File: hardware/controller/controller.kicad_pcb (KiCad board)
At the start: 2 copper layers, 30 parts, among them J1 Conn_01x02_Pin, J10 Conn_01x04_Pin, J11 Barrel_Jack, J2 Conn_01x02_Pin, J3 Conn_01x02_Pin, J4 Conn_01x02_Pin, J5 Screw_Terminal_01x02, J6 Screw_Terminal_01x02, J7 Conn_01x04_Pin, J8 Conn_01x04_Pin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

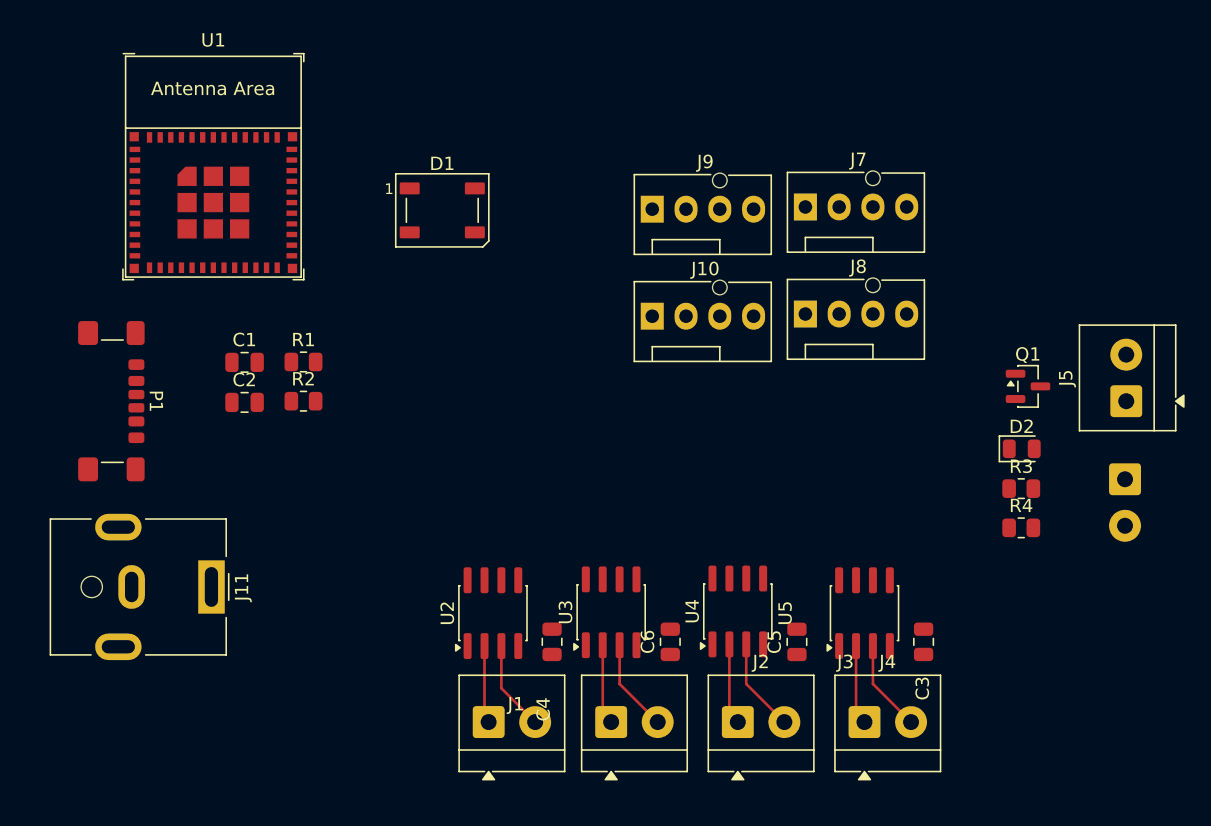
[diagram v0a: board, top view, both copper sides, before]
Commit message: Fixed up MCU strapping pins
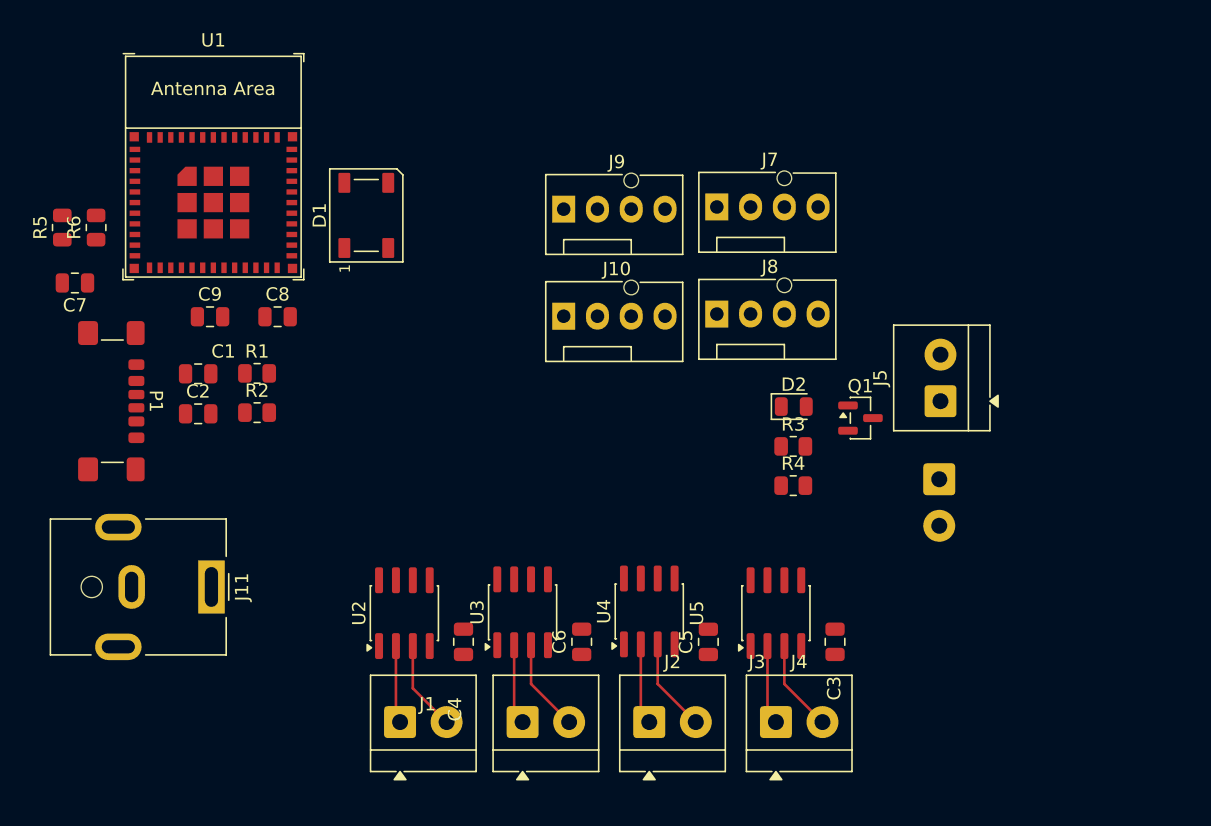
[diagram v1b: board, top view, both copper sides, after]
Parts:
- added C7: 10uF, Capacitor_SMD:C_0805_2012Metric, F.Cu at (110.2, 81.3)
- added C8: 1uF, Capacitor_SMD:C_0805_2012Metric, F.Cu at (125.4, 83.8)
- added C9: 0.1uf, Capacitor_SMD:C_0805_2012Metric, F.Cu at (120.3, 83.8)
- added R5: 10K, Resistor_SMD:R_0805_2012Metric, F.Cu at (109.2, 77.1)
- added R6: R_US, Resistor_SMD:R_0805_2012Metric, F.Cu at (111.8, 77.1)
- moved R3 17.4 mm to (164.2, 93.6)
- moved D2 17.4 mm to (164.2, 90.6)
- moved R4 17.4 mm to (164.2, 96.5)
- moved J5 14.0 mm to (175.3, 90.2)
- moved J6 14.0 mm to (175.2, 96.0)
- moved Q1 12.8 mm to (169.2, 91.4)
- moved C4 6.66 mm to (139.4, 108.3)
- moved C3 6.66 mm to (167.3, 108.3)
- moved C5 6.66 mm to (157.8, 108.3)
- moved C6 6.66 mm to (148.3, 108.3)
- moved J1 6.66 mm to (134.6, 114.3)
- moved J10 6.66 mm to (146.9, 83.8)
- moved J2 6.66 mm to (143.8, 114.3)
- moved J3 6.66 mm to (153.4, 114.3)
- moved J4 6.66 mm to (162.9, 114.3)
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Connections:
- C1 pad 1: /Microcontroller/D- -> Net-(P1-D-)
- C2 pad 1: /Microcontroller/D+ -> Net-(P1-D+)
- R1 pad 1: Net-(U1-GPIO19/USB_D+) -> /Microcontroller/USB_D-
- R1 pad 2: /Microcontroller/D+ -> Net-(P1-D-)
- R2 pad 1: Net-(U1-GPIO18/USB_D-) -> /Microcontroller/USB_D+
- R2 pad 2: /Microcontroller/D- -> Net-(P1-D+)
- U1 pad 26: Net-(U1-GPIO18/USB_D-) -> /Microcontroller/USB_D-
- U1 pad 27: Net-(U1-GPIO19/USB_D+) -> /Microcontroller/USB_D+
- U1 pad 5: unconnected-(U1-GPIO2/ADC1_CH2-Pad5) -> Net-(U1-GPIO2/ADC1_CH2)
- U1 pad 8: unconnected-(U1-EN/CHIP_PU-Pad8) -> Net-(U1-EN/CHIP_PU)

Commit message: Filled out power section of schematic
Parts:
- removed Q1: MMBF4392, Package_TO_SOT_SMD:SOT-23
- added C10: 22uF, Capacitor_SMD:C_0805_2012Metric, F.Cu at (130.2, 91.2)
- added C11: 10uF, Capacitor_SMD:C_0805_2012Metric, F.Cu at (130.2, 94.2)
- added R10: 100k, Resistor_SMD:R_0805_2012Metric, F.Cu at (135.0, 92.1)
- added R4: 33k, Resistor_SMD:R_0805_2012Metric, F.Cu at (135.0, 83.2)
- added R7: 5.1k, Resistor_SMD:R_0805_2012Metric, F.Cu at (119.4, 94.0)
- added R8: 75k, Resistor_SMD:R_0805_2012Metric, F.Cu at (135.0, 86.2)
- added R9: 75k, Resistor_SMD:R_0805_2012Metric, F.Cu at (135.0, 89.1)
- added U6: TPS1H200AQDGNRQ1, TPS1H200:SOP65P490X110-9N, F.Cu at (168.6, 92.5)
- added U7: MPM3606AGQV-P, MPM3606:QFN3p0x5p0x1p6_MPM3606A_MNP, F.Cu at (127.4, 100.1)
- added U8: LM73100RPWR, LM73100:IC_LM73100RPWR, F.Cu at (130.8, 83.7)
- added U9: LM73100RPWR, LM73100:IC_LM73100RPWR, F.Cu at (130.8, 87.7)
- C3, C4, C5, C6: value C -> 0.1uf
- R1, R2: value R_US -> 33
- R3, R4: value R_US -> 500
- R6: value R_US -> 10k
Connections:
- J6 pad 1: +12V -> Net-(J6-Pin_1)
- J6 pad 2: Net-(J6-Pin_2) -> GND
- P1 pad A5: unconnected-(P1-CC-PadA5) -> Net-(P1-CC)

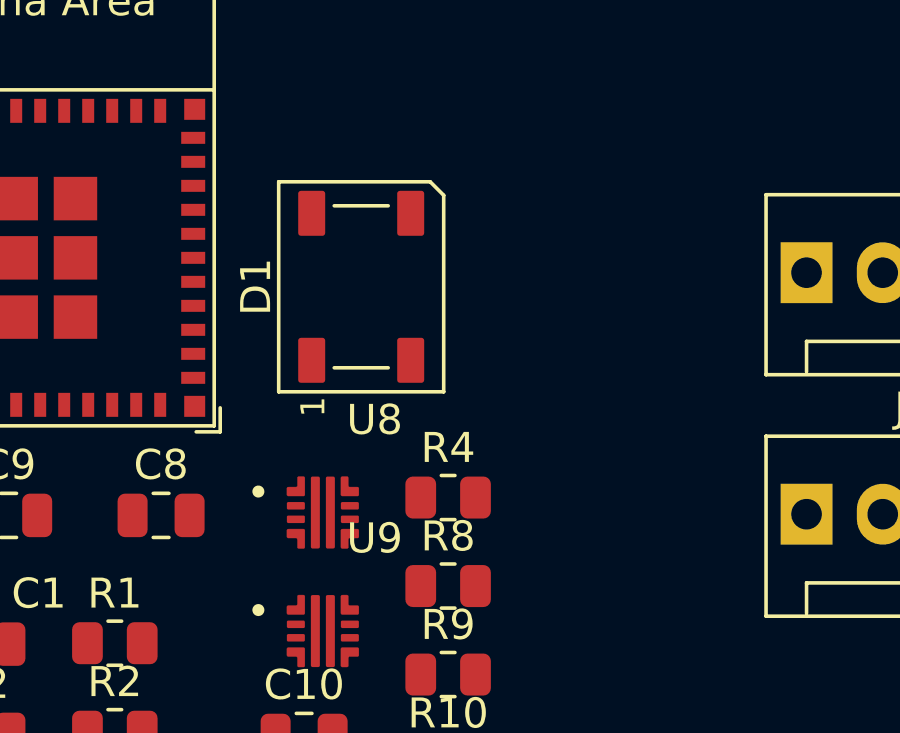
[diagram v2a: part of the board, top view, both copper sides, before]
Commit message: Fix USB symbol, adjust decoupling caps
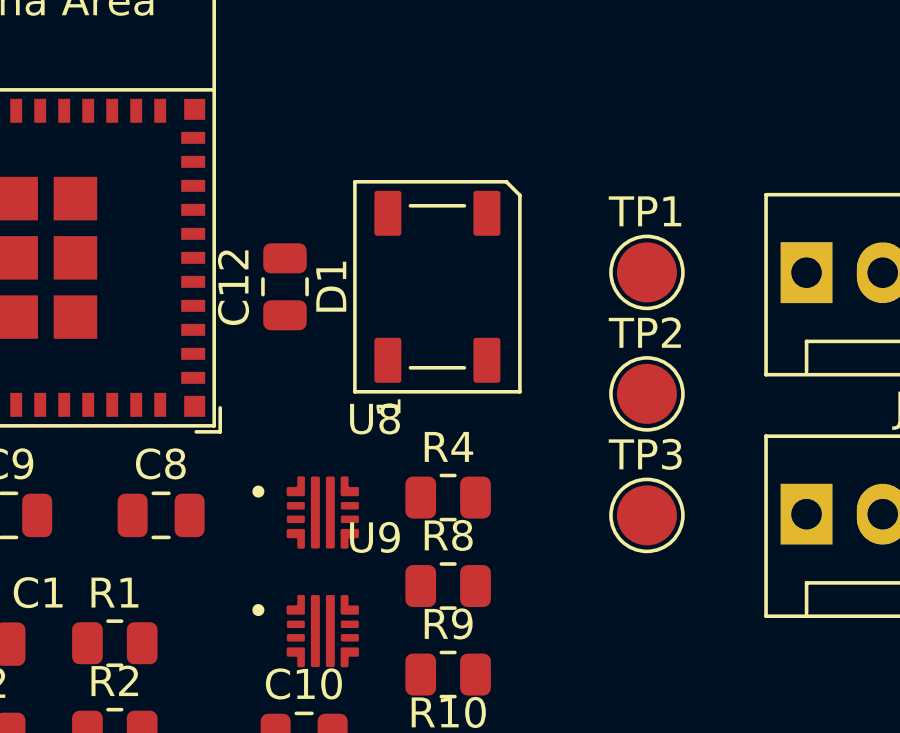
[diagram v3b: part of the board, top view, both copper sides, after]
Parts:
- added C12: 0.1uf, Capacitor_SMD:C_0805_2012Metric, F.Cu at (129.5, 76.2)
- added TP1: TestPoint, TestPoint:TestPoint_Pad_D2.0mm, F.Cu at (141.6, 75.7)
- added TP2: TestPoint, TestPoint:TestPoint_Pad_D2.0mm, F.Cu at (141.6, 79.8)
- added TP3: TestPoint, TestPoint:TestPoint_Pad_D2.0mm, F.Cu at (141.6, 83.8)
- moved D1 2.54 mm to (134.6, 76.2)
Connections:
- P1 pad A12: GND -> Net-(P1-GND-PadA1)
- P1 pad B12: GND -> Net-(P1-GND-PadA1)
- P1 pad S1: GND -> unconnected-(P1-SHIELD-PadS1)
- U6 pad 2: unconnected-(U6-DIAG_EN-Pad2) -> /Microcontroller/HEATER
- U6 pad 9: unconnected-(U6-EP-Pad9) -> GND
- U7 pad 4: unconnected-(U7-SW-Pad4) -> /Power/V_SW
- U7 pad 5: unconnected-(U7-SW-Pad5) -> /Power/V_SW
- U7 pad 6: unconnected-(U7-SW-Pad6) -> /Power/V_SW

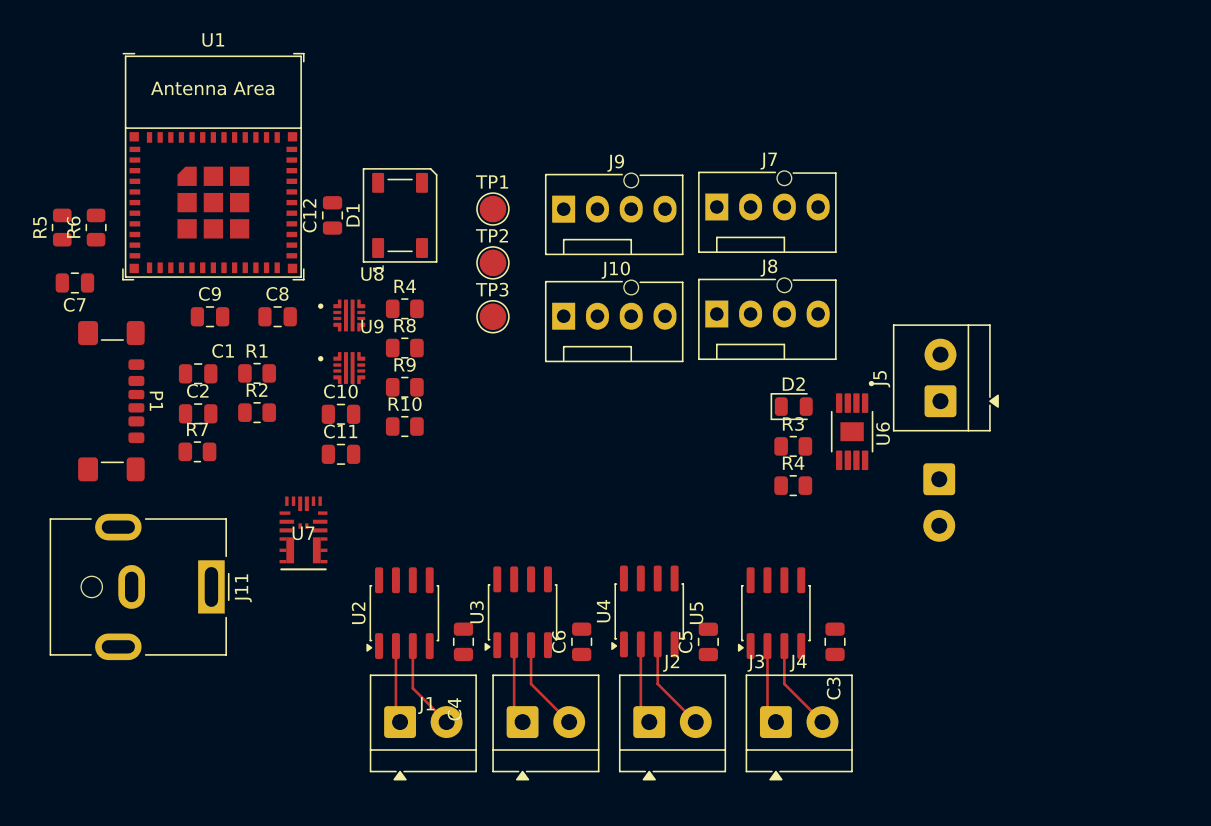
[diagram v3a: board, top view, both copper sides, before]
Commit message: Drop to 3x thermocouples, 2x fans
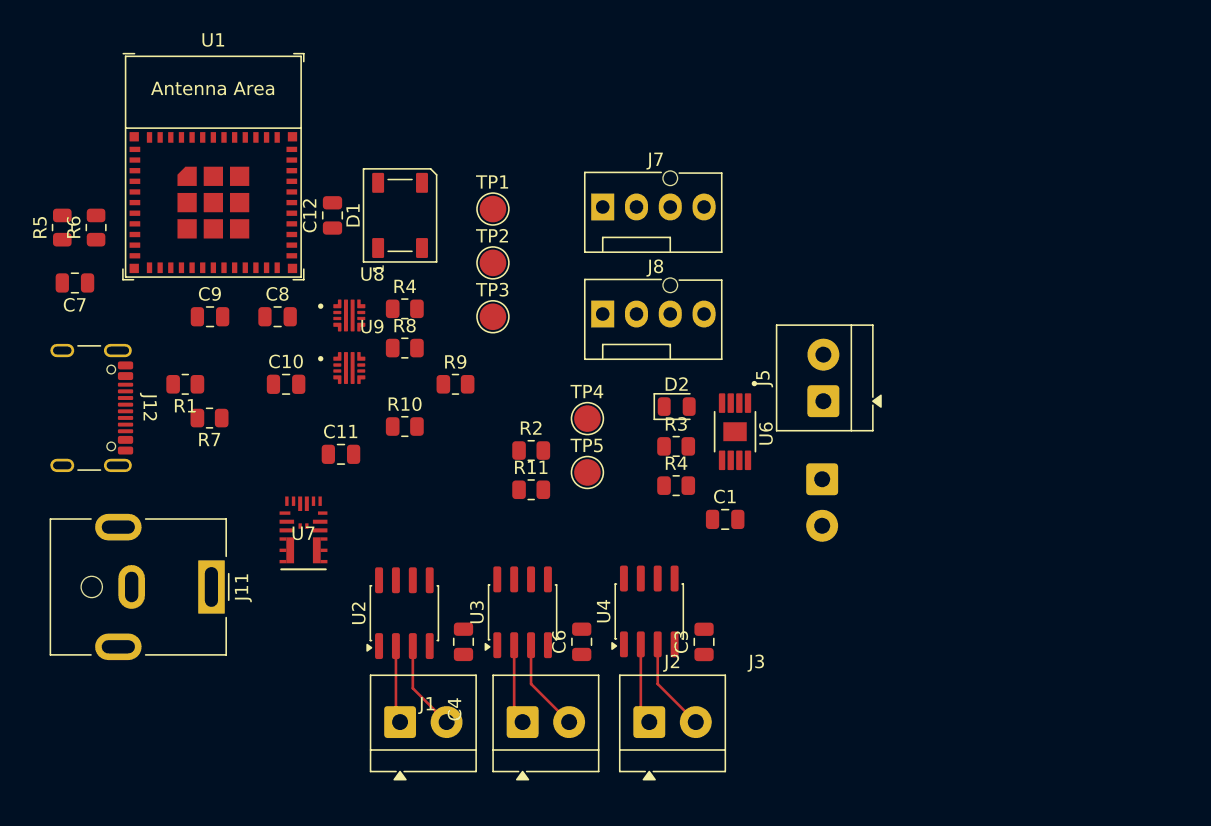
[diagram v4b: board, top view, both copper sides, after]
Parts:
- removed C2: C, Capacitor_SMD:C_0805_2012Metric
- removed C5: 0.1uf, Capacitor_SMD:C_0805_2012Metric
- removed J10, J9: Conn_01x04_Pin, Connector:FanPinHeader_1x04_P2.54mm_Vertical
- removed J4: Conn_01x02_Pin, TerminalBlock_4Ucon:TerminalBlock_4Ucon_1x02_P3.50mm_Horizontal
- removed P1: USB_C_Plug_USB2.0, Connector_USB:USB_C_Receptacle_GCT_USB4135-GF-A_6P_TopMnt_Horizontal
- removed U5: MAX31855KASA, Package_SO:SOIC-8_3.9x4.9mm_P1.27mm
- added J12: USB_C_Receptacle_USB2.0_14P, Connector_USB:USB_C_Receptacle_GCT_USB4105-xx-A_16P_TopMnt_Horizontal, F.Cu at (110.3, 90.7)
- added R11: 10k, Resistor_SMD:R_0805_2012Metric, F.Cu at (144.5, 96.8)
- added TP4: TestPoint, TestPoint:TestPoint_Pad_D2.0mm, F.Cu at (148.7, 91.5)
- added TP5: TestPoint, TestPoint:TestPoint_Pad_D2.0mm, F.Cu at (148.7, 95.5)
- C1: value C -> 0.1uF
- C12, C3, C4, C6: value 0.1uf -> 1uF
- R1: value 33 -> 5.1k
- R2: value 33 -> 10k
- moved C1 41.1 mm to (159.1, 99.1)
- moved R2 20.8 mm to (144.5, 93.9)
- moved C3 9.85 mm to (157.5, 108.3)
- moved R3 8.81 mm to (155.4, 93.6)
- moved R4 8.81 mm to (155.4, 96.5)
- moved U6 8.81 mm to (159.8, 92.5)
- moved D2 8.80 mm to (155.4, 90.6)
- moved J5 8.80 mm to (166.5, 90.2)
- moved J6 8.80 mm to (166.4, 96.0)
- moved J7 8.58 mm to (149.9, 75.6)
- moved J8 8.58 mm to (149.9, 83.6)
- moved R1 5.46 mm to (118.5, 88.9), turned to 180 degrees
- moved C10 4.70 mm to (126.0, 88.9)
- moved R9 3.82 mm to (138.8, 88.9)
- moved R7 2.70 mm to (120.3, 91.4), turned to 180 degrees
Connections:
- C1 pad 1: Net-(P1-D-) -> +12V
- J7 pad 3: unconnected-(J7-Pin_3-Pad3) -> FAN_0_TACH
- J8 pad 3: unconnected-(J8-Pin_3-Pad3) -> FAN_1_TACH
- R1 pad 1: /Microcontroller/USB_D- -> GND
- R1 pad 2: Net-(P1-D-) -> Net-(J12-CC1)
- R2 pad 1: /Microcontroller/USB_D+ -> FAN_0_TACH
- R2 pad 2: Net-(P1-D+) -> +3V3
- U1 pad 16: CS3 -> SO
- U1 pad 30: unconnected-(U1-GPIO20/U0RXD-Pad30) -> FAN_1_TACH
- U1 pad 31: unconnected-(U1-GPIO21/U0TXD-Pad31) -> FAN_0_TACH
- U1 pad 6: SO -> unconnected-(U1-GPIO3/ADC1_CH3-Pad6)
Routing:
- net Net-(J4-Pin_2): track 6.90 -> 0.00 mm
- net Net-(J4-Pin_1): track 5.98 -> 0.00 mm

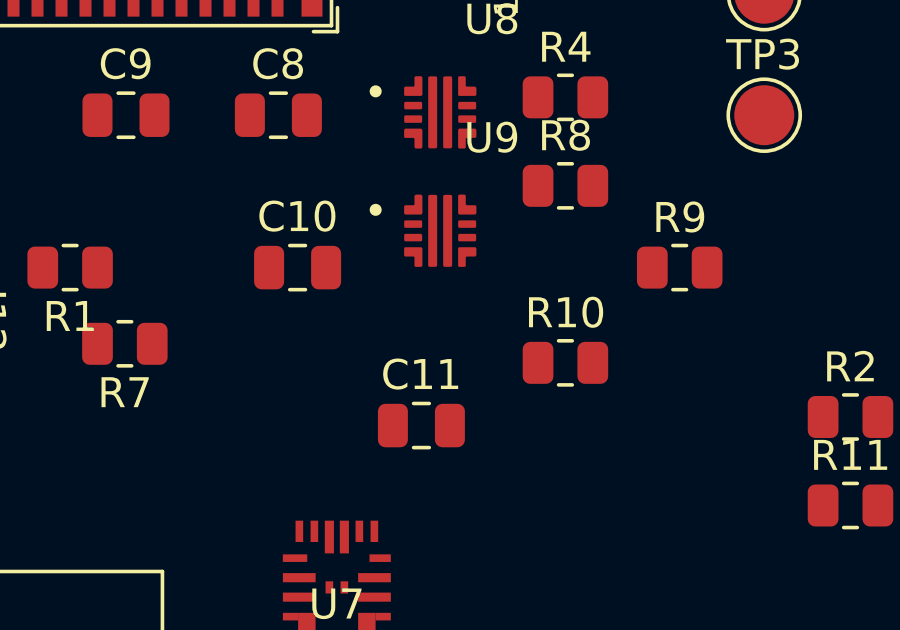
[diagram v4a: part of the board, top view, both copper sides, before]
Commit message: Add more decoupling caps
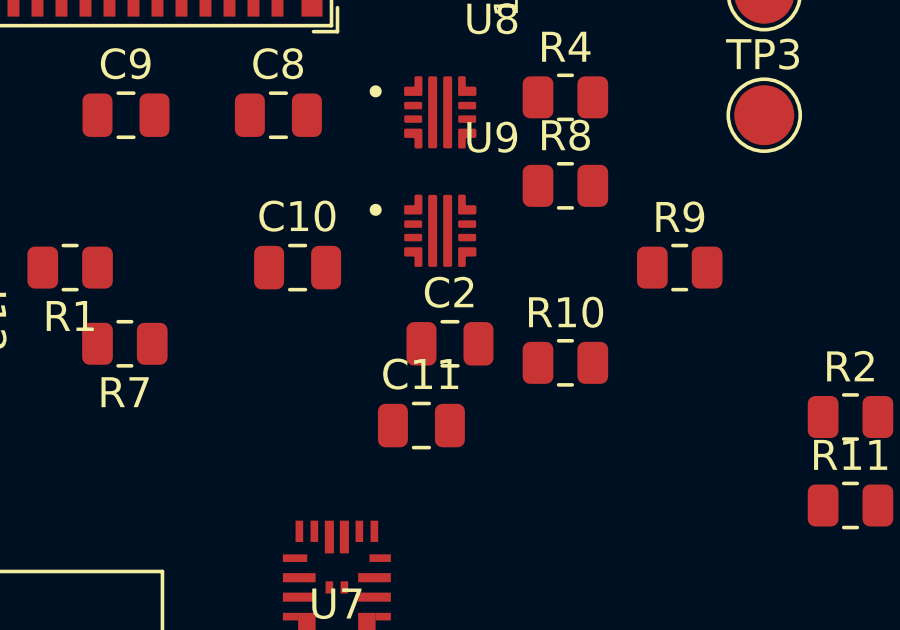
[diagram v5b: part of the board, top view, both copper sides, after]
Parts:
- added C2: 10uF, Capacitor_SMD:C_0805_2012Metric, F.Cu at (131.1, 91.4)
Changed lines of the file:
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@@
+		)
+	)
+	(footprint "Capacitor_SMD:C_0805_2012Metric"
+		(layer "F.Cu")
+		(at 131.13 91.44)
+		(descr "Capacitor SMD 0805 (2012 Metric), square (rectangular) end terminal, IPC-7351 nominal, (Body size source: IPC-SM-782 page 76, https://www.pcb-3d.com/wordpress/wp-content/uploads/ipc-sm-782a_amendment_1_and_2.pdf, https://docs.google.com/spreadsheets/d/1BsfQQcO9C6DZCsRaXUlFlo91Tg2WpOkGARC1WS5S8t0/edit?usp=sharing), generated with kicad-footprint-generator")
+		(tags "capacitor")
+		(property "Reference" "C2"
+			(at 0 -1.68 0)
+			(layer "F.SilkS")
+			(effects
+				(font
+					(size 1 1)
+					(thickness 0.15)
+				)
+			)
+		)
+		(property "Value" "10uF"
+			(at 0 1.68 0)
+			(layer "F.Fab")
+			(effects
+				(font
+					(size 1 1)
+					(thickness 0.15)
+				)
+			)
+		)
+		(property "Datasheet" "~"
+			(at 0 0 0)
+			(layer "F.Fab")
+			(hide yes)
+			(effects
+				(font
+					(size 1.27 1.27)
+					(thickness 0.15)
+				)
+			)
+		)
+		(property "Description" "Unpolarized capacitor"
+			(at 0 0 0)
+			(layer "F.Fab")
+			(hide yes)
+			(effects
+				(font
+					(size 1.27 1.27)
+					(thickness 0.15)
+				)
+			)
+		)
+		(property ki_fp_filters "C_*")
+		(sheetname "/Power/")
+		(sheetfile "power.kicad_sch")
+		(attr smd)
+		(fp_line
+			(start -0.261252 -0.735)
+			(end 0.261252 -0.735)
+			(stroke
+				(width 0.12)
+				(type solid)
+			)
+			(layer "F.SilkS")
+		)
+		(fp_line
+			(start -0.261252 0.735)
+			(end 0.261252 0.735)
+			(stroke
+				(width 0.12)
+				(type solid)
+			)
+			(layer "F.SilkS")
+		)
+		(fp_line
+			(start -1.7 -0.98)
+			(end 1.7 -0.98)
+			(stroke
+				(width 0.05)
+				(type solid)
+			)
+			(layer "F.CrtYd")
+		)
+		(fp_line
+			(start -1.7 0.98)
+			(end -1.7 -0.98)
+			(stroke
+				(width 0.05)
+				(type solid)
+			)
+			(layer "F.CrtYd")
+		)
+		(fp_line
+			(start 1.7 -0.98)
+			(end 1.7 0.98)
+			(stroke
+				(width 0.05)
+				(type solid)
+			)
+			(layer "F.CrtYd")
+		)
+		(fp_line
+			(start 1.7 0.98)
+			(end -1.7 0.98)
+			(stroke
+				(width 0.05)
+				(type solid)
+			)
+			(layer "F.CrtYd")
+		)
+		(fp_line
+			(start -1 -0.625)
+			(end 1 -0.625)
+			(stroke
+				(width 0.1)
+				(type solid)
+			)
+			(layer "F.Fab")
+		)
+		(fp_line
+			(start -1 0.625)
+			(end -1 -0.625)
+			(stroke
+				(width 0.1)
+				(type solid)
+			)
+			(layer "F.Fab")
+		)
+		(fp_line
+			(start 1 -0.625)
+			(end 1 0.625)
+			(stroke
+				(width 0.1)
+				(type solid)
+			)
+			(layer "F.Fab")
+		)
+		(fp_line
+			(start 1 0.625)
+			(end -1 0.625)
+			(stroke
+				(width 0.1)
+				(type solid)
+			)
+			(layer "F.Fab")
+		)
+		(fp_text user "${REFERENCE}"
+			(at 0 0 0)
+			(layer "F.Fab")
+			(effects
+				(font
+					(size 0.5 0.5)
+					(thickness 0.08)
+				)
+			)
+		)
+		(pad "1" smd roundrect
+			(at -0.95 0)
+			(size 1 1.45)
+			(layers "F.Cu" "F.Mask" "F.Paste")
+			(roundrect_rratio 0.25)
+			(net 39 "+12V")
+			(pintype "passive")
+		)
+		(pad "2" smd roundrect
+			(at 0.95 0)
+			(size 1 1.45)
+			(layers "F.Cu" "F.Mask" "F.Paste")
+			(roundrect_rratio 0.25)
+			(net 18 "GND")
+			(pintype "passive")
+		)
+		(embedded_fonts no)
+		(model "${KICAD9_3DMODEL_DIR}/Capacitor_SMD.3dshapes/C_0805_2012Metric.step"
+			(offset
+				(xyz 0 0 0)
+			)
+			(scale
+				(xyz 1 1 1)
+			)
+			(rotate
+				(xyz 0 0 0)
+			)
 		)
 	)
